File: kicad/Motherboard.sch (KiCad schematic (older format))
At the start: 0 parts

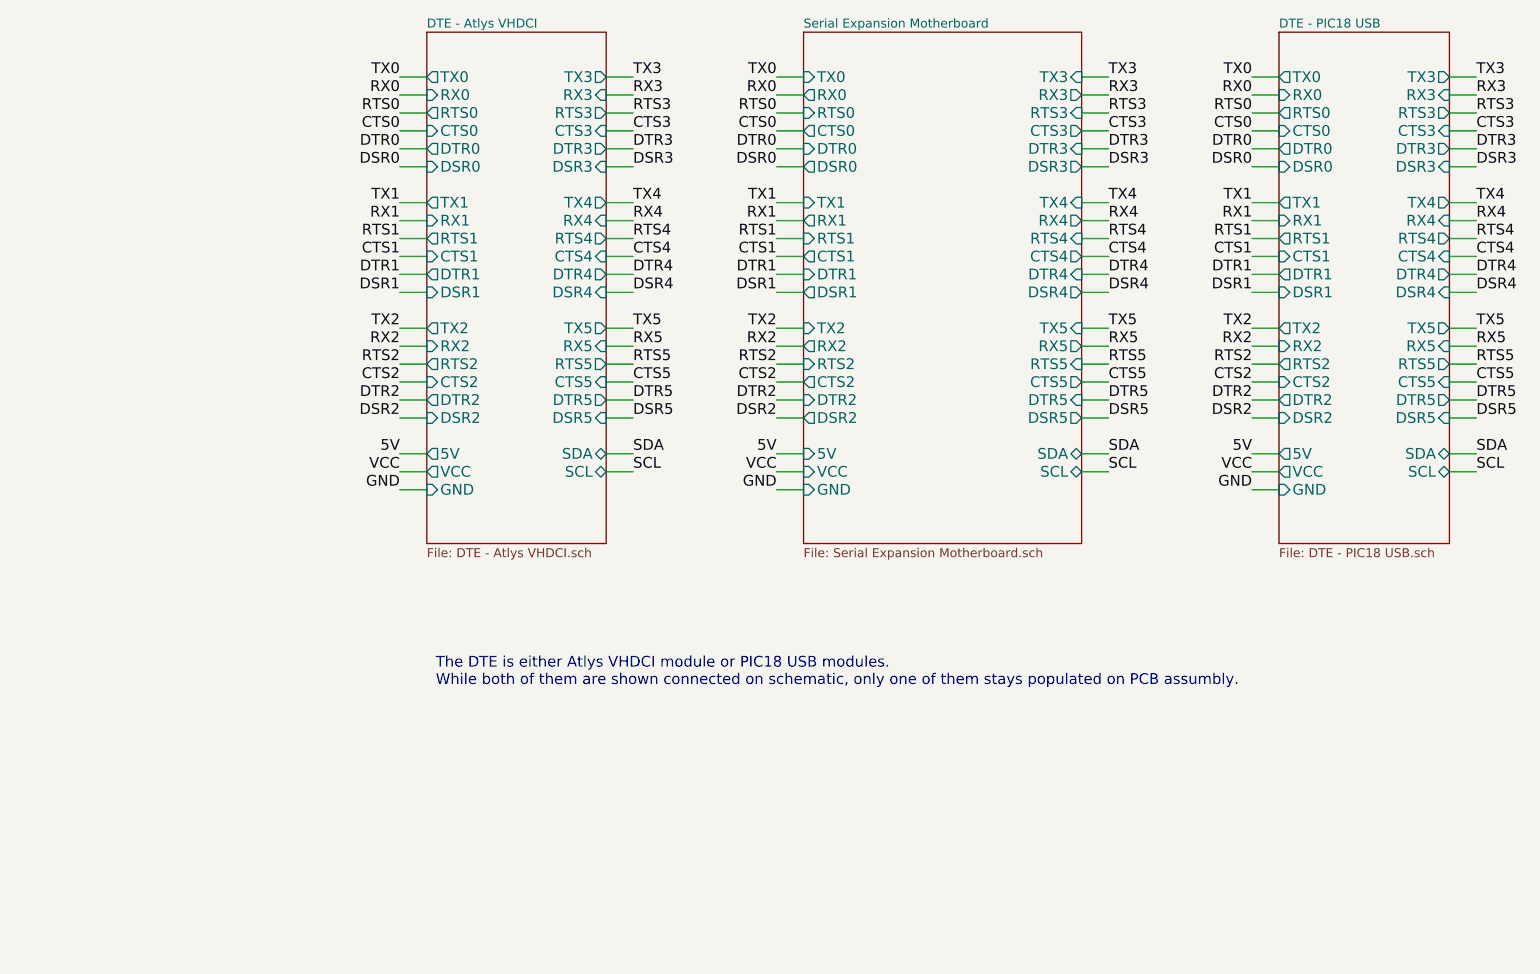
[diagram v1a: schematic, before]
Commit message: Updated notes and sheet names
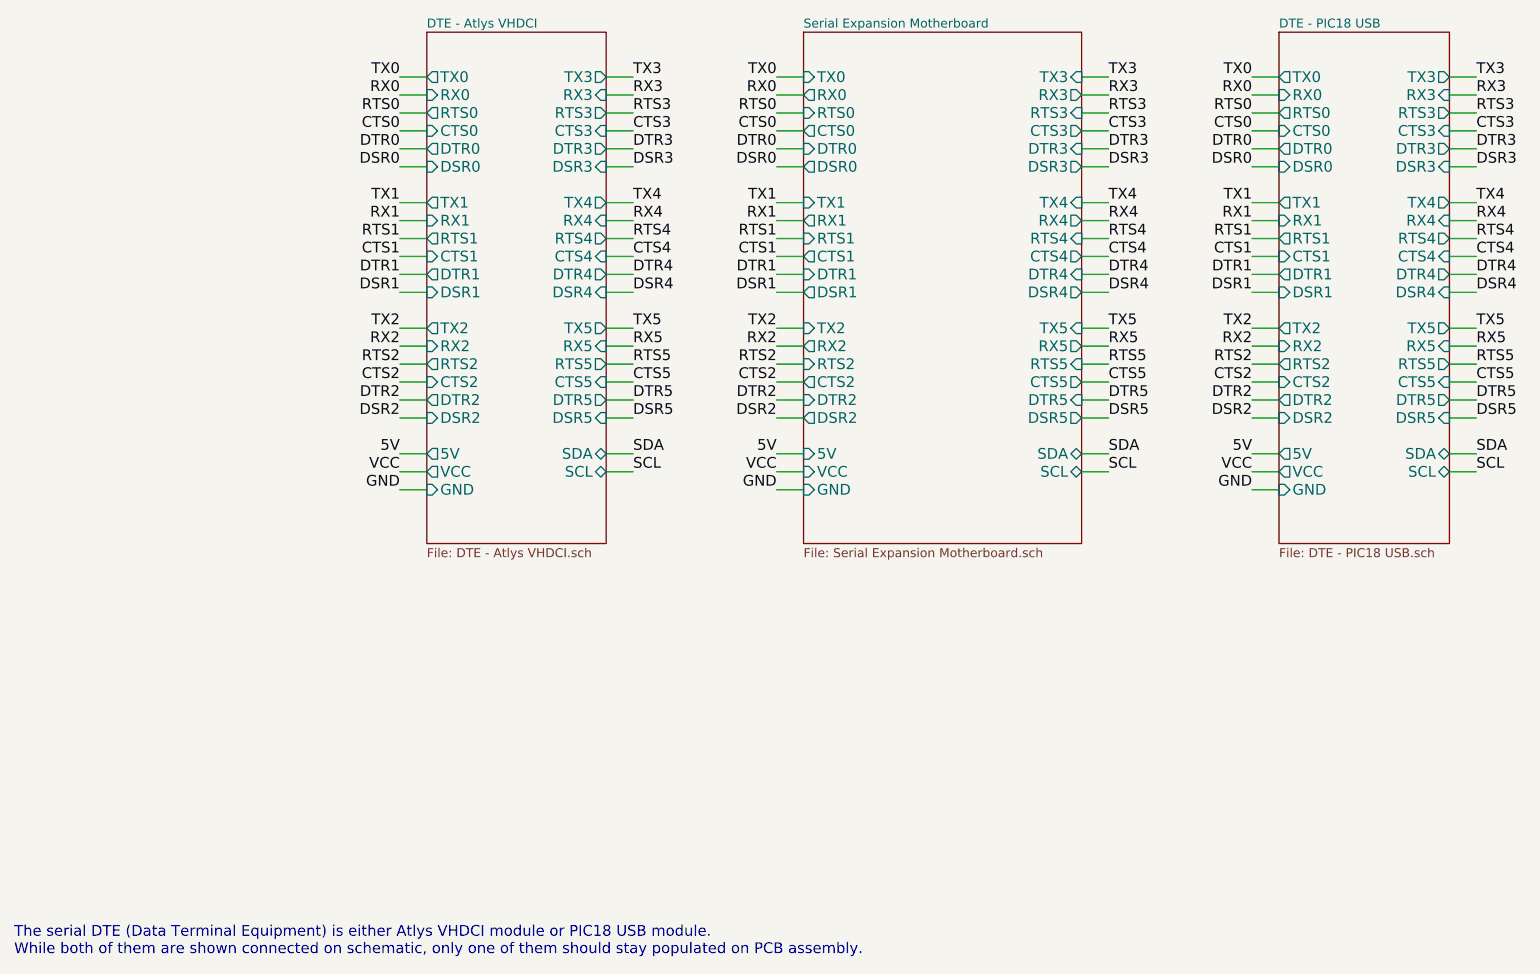
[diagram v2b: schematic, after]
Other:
- note added: "The serial DTE (Data Terminal Equipment) is either Atlys VHDCI module or PIC18 USB module.\nWhile both of them are shown connected on schematic, only one of them should stay populated on PCB assembly."
- note removed: "The DTE is either Atlys VHDCI module or PIC18 USB modules.\nWhile both of them are shown connected on schematic, only one of them stays populated on PCB assumbly."
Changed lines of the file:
@@
 encoding utf-8
 Sheet 1 7
-Title "noname.sch"
+Title "Serial Expansion Module and DTE interface"
 Date "23 jun 2014"
 Rev ""
-Comp ""
+Comp "TimVideos"
 Comment1 ""
 Comment2 ""
@@
 F42 "DSR5" O R 6900 4550 60
 $EndSheet
-Text Notes 3300 6050 0    60   ~ 0
-The DTE is either Atlys VHDCI module or PIC18 USB modules.\nWhile both of them are shown connected on schematic, only one of them stays populated on PCB assumbly.
+Text Notes 950  7550 0    60   ~ 0
+The serial DTE (Data Terminal Equipment) is either Atlys VHDCI module or PIC18 USB module.\nWhile both of them are shown connected on schematic, only one of them should stay populated on PCB assembly.
 Wire Wire Line
 	5350 2650 5200 2650
